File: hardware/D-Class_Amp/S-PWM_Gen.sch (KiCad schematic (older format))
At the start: 11 parts, among them U501 MAX4016, U502 Comparator_Dual_Generic

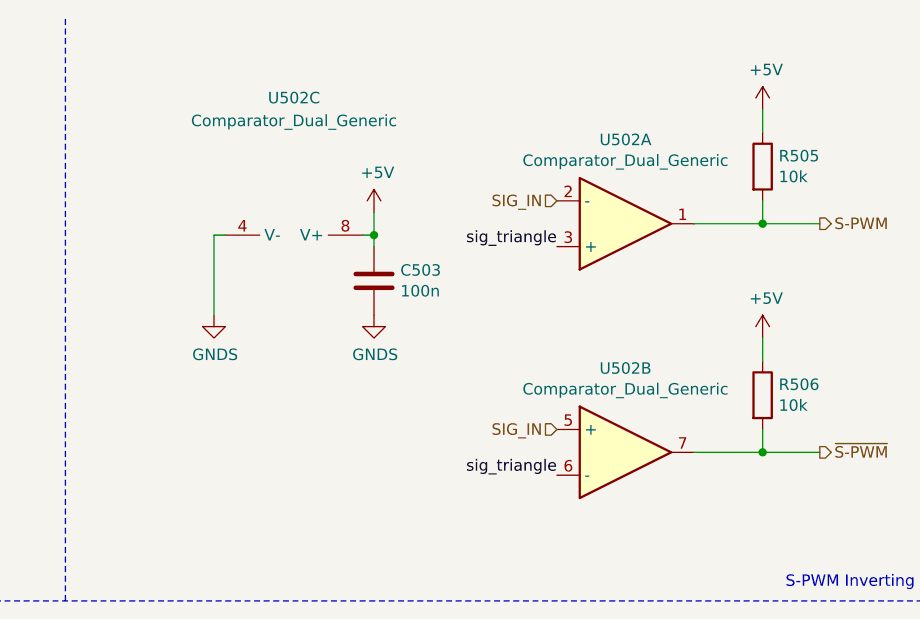
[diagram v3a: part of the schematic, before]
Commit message: select comparator and set footprint
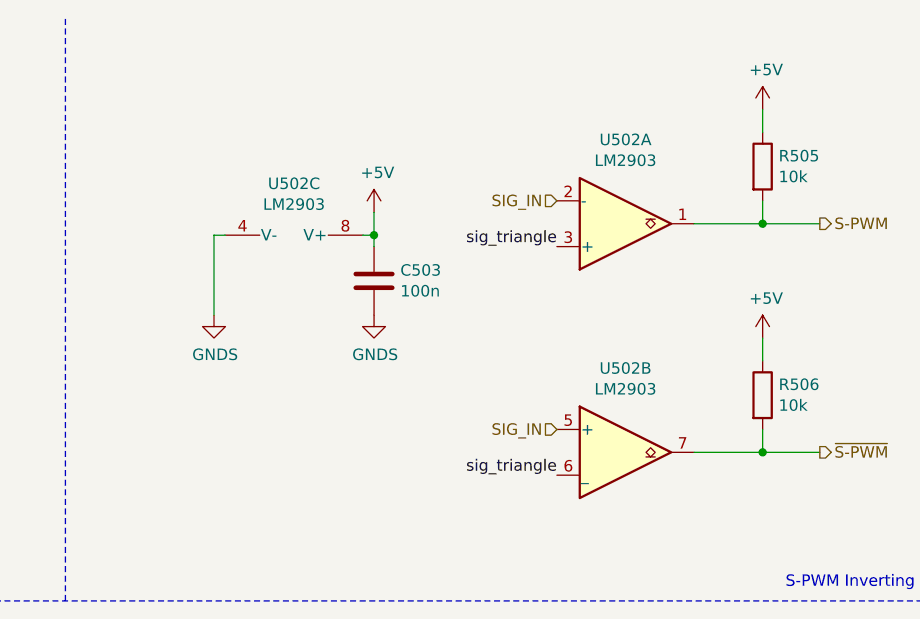
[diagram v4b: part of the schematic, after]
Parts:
- removed U502: Comparator_Dual_Generic, symbol Device:Opamp_Dual_Generic
- added U502: LM2903, Package_SO:SOIC-8_3.9x4.9mm_P1.27mm, symbol Comparator:LM2903
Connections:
- net +5V: now also U502.8 (V+)
- net GNDS: now also U502.4 (V-)
- net S-PWM: now also U502.1
- net SIG_IN: now also U502.2 (-), U502.5 (+)
- net sig_triangle: now also U502.3 (+), U502.6 (_)
- net ~S-PWM: now also U502.7
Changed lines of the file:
@@
 Text Label 5325 1925 2    50   ~ 0
 sig_triangle
-Text HLabel 9600 1375 2    50   Output ~ 0
-S-PWM
 Text HLabel 9600 2375 2    50   Output ~ 0
 ~S-PWM
-$Comp
-L Device:Opamp_Dual_Generic U502
-U 1 1 610E84D1
-P 8750 1375
-F 0 "U502" H 8750 1008 50  0000 C CNN
-F 1 "Comparator_Dual_Generic" H 8750 1099 50  0000 C CNN
-F 2 "" H 8750 1375 50  0001 C CNN
-F 3 "~" H 8750 1375 50  0001 C CNN
-	1    8750 1375
-	1    0    0    1
-$EndComp
-$Comp
-L Device:Opamp_Dual_Generic U502
-U 2 1 610E8A2F
-P 8750 2375
-F 0 "U502" H 8750 2742 50  0000 C CNN
-F 1 "Comparator_Dual_Generic" H 8750 2651 50  0000 C CNN
-F 2 "" H 8750 2375 50  0001 C CNN
-F 3 "~" H 8750 2375 50  0001 C CNN
-	2    8750 2375
-	1    0    0    -1
-$EndComp
 $Comp
 L Device:C C503
@@
 	1    0    0    -1
 $EndComp
-$Comp
-L Device:Opamp_Dual_Generic U502
-U 3 1 610E9B4A
-P 7300 1525
-F 0 "U502" V 6600 1525 50  0000 C CNN
-F 1 "Comparator_Dual_Generic" V 6700 1525 50  0000 C CNN
-F 2 "" H 7300 1525 50  0001 C CNN
-F 3 "~" H 7300 1525 50  0001 C CNN
-	3    7300 1525
-	0    1    1    0
-$EndComp
 Wire Wire Line
 	7650 1475 7650 1425
@@
 Text HLabel 8450 2275 0    50   Input ~ 0
 SIG_IN
-Text HLabel 8450 1275 0    50   Input ~ 0
-SIG_IN
-Text Label 8450 1475 2    50   ~ 0
-sig_triangle
 Text Label 8450 2475 2    50   ~ 0
 sig_triangle
-Wire Wire Line
-	9050 1375 9350 1375
-$Comp
-L Device:R R505
-U 1 1 6112AEF0
-P 9350 1125
-F 0 "R505" H 9420 1171 50  0000 L CNN
-F 1 "10k" H 9420 1080 50  0000 L CNN
-F 2 "Resistor_SMD:R_0805_2012Metric_Pad1.20x1.40mm_HandSolder" V 9280 1125 50  0001 C CNN
-F 3 "~" H 9350 1125 50  0001 C CNN
-	1    9350 1125
-	1    0    0    -1
-$EndComp
-Wire Wire Line
-	9350 1275 9350 1375
-Connection ~ 9350 1375
-Wire Wire Line
-	9350 1375 9600 1375
-$Comp
-L power:+5V #PWR0509
-U 1 1 61133A73
-P 9350 875
-F 0 "#PWR0509" H 9350 725 50  0001 C CNN
-F 1 "+5V" H 9365 1048 50  0000 C CNN
-F 2 "" H 9350 875 50  0001 C CNN
-F 3 "" H 9350 875 50  0001 C CNN
-	1    9350 875
-	1    0    0    -1
-$EndComp
-Wire Wire Line
-	9350 875  9350 975
 Wire Wire Line
 	9050 2375 9350 2375
@@
 Wire Wire Line
 	4025 2025 4075 2025
+$Comp
+L Comparator:LM2903 U502
+U 3 1 610EF685
+P 7300 1525
+F 0 "U502" V 6975 1525 50  0000 C CNN
+F 1 "LM2903" V 7066 1525 50  0000 C CNN
+F 2 "Package_SO:SOIC-8_3.9x4.9mm_P1.27mm" H 7300 1525 50  0001 C CNN
+F 3 "http://www.ti.com/lit/ds/symlink/lm393.pdf" H 7300 1525 50  0001 C CNN
+	3    7300 1525
+	0    1    1    0
+$EndComp
+$Comp
+L Comparator:LM2903 U502
+U 2 1 610F0244
+P 8750 2375
+F 0 "U502" H 8750 2742 50  0000 C CNN
+F 1 "LM2903" H 8750 2651 50  0000 C CNN
+F 2 "Package_SO:SOIC-8_3.9x4.9mm_P1.27mm" H 8750 2375 50  0001 C CNN
+F 3 "http://www.ti.com/lit/ds/symlink/lm393.pdf" H 8750 2375 50  0001 C CNN
+	2    8750 2375
+	1    0    0    -1
+$EndComp
+$Comp
+L Comparator:LM2903 U502
+U 1 1 610ED916
+P 8750 1375
+F 0 "U502" H 8750 1008 50  0000 C CNN
+F 1 "LM2903" H 8750 1099 50  0000 C CNN
+F 2 "Package_SO:SOIC-8_3.9x4.9mm_P1.27mm" H 8750 1375 50  0001 C CNN
+F 3 "http://www.ti.com/lit/ds/symlink/lm393.pdf" H 8750 1375 50  0001 C CNN
+	1    8750 1375
+	1    0    0    1
+$EndComp
+Wire Wire Line
+	9350 875  9350 975
+$Comp
+L power:+5V #PWR0509
+U 1 1 61133A73
+P 9350 875
+F 0 "#PWR0509" H 9350 725 50  0001 C CNN
+F 1 "+5V" H 9365 1048 50  0000 C CNN
+F 2 "" H 9350 875 50  0001 C CNN
+F 3 "" H 9350 875 50  0001 C CNN
+	1    9350 875
+	1    0    0    -1
+$EndComp
+Wire Wire Line
+	9350 1375 9600 1375
+Connection ~ 9350 1375
+Wire Wire Line
+	9350 1275 9350 1375
+$Comp
+L Device:R R505
+U 1 1 6112AEF0
+P 9350 1125
+F 0 "R505" H 9420 1171 50  0000 L CNN
+F 1 "10k" H 9420 1080 50  0000 L CNN
+F 2 "Resistor_SMD:R_0805_2012Metric_Pad1.20x1.40mm_HandSolder" V 9280 1125 50  0001 C CNN
+F 3 "~" H 9350 1125 50  0001 C CNN
+	1    9350 1125
+	1    0    0    -1
+$EndComp
+Wire Wire Line
+	9050 1375 9350 1375
+Text Label 8450 1475 2    50   ~ 0
+sig_triangle
+Text HLabel 8450 1275 0    50   Input ~ 0
+SIG_IN
+Text HLabel 9600 1375 2    50   Output ~ 0
+S-PWM
 $EndSCHEMATC

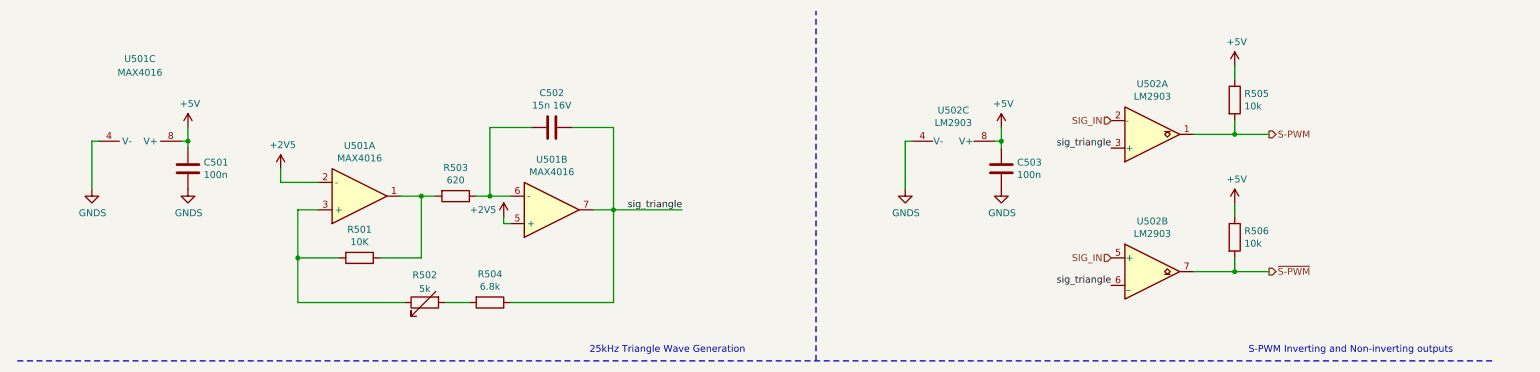
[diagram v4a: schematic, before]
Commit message: updated SPWM model with new comparators, also added test points to schematic and fixed MOSFET footprints
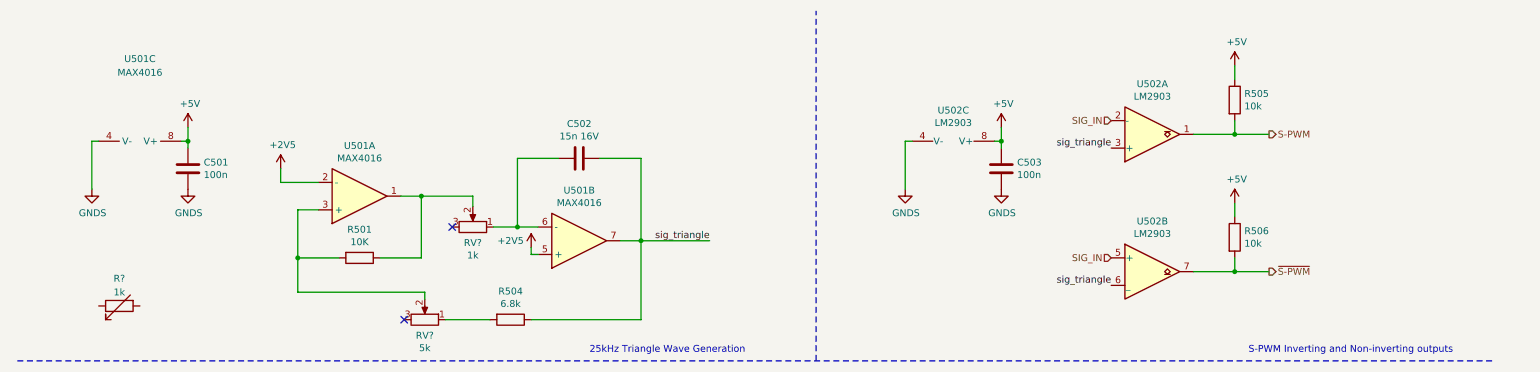
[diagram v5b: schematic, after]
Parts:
- removed R502: 5k, Potentiometer_THT:Potentiometer_Vishay_T73YP_Vertical, symbol Device:R_Variable
- removed R503: 620, Resistor_SMD:R_0805_2012Metric_Pad1.20x1.40mm_HandSolder, symbol Device:R
- added R?: 1k, Potentiometer_THT:Potentiometer_Vishay_T73YP_Vertical, symbol Device:R_Variable
- added RV?: 5k, Potentiometer_THT:Potentiometer_Vishay_T73YP_Vertical, symbol Device:R_POT
- added RV?: 1k, Potentiometer_THT:Potentiometer_Vishay_T73YP_Vertical, symbol Device:R_POT
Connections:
- net at R501.1, U501.1: now also RV?.2
- net at R501.2, U501.3 (+): now also RV?.2
- net at C502.2, U501.6 (-): now also RV?.1
- net at R504.2: now also RV?.1
- no-connect marks 0 -> 2
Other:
- moved on the sheet: C502, R504, U501B
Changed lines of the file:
@@
 $Descr A4 11693 8268
 encoding utf-8
-Sheet 5 5
+Sheet 3 5
 Title "S-PWM Generator "
 Date ""
@@
 L Device:Opamp_Dual_Generic U501
 U 2 1 6104BF37
-P 4375 1925
-F 0 "U501" H 4375 1558 50  0000 C CNN
-F 1 "MAX4016" H 4375 1649 50  0000 C CNN
-F 2 "Package_SO:SOIC-8_3.9x4.9mm_P1.27mm" H 4375 1925 50  0001 C CNN
-F 3 "https://datasheets.maximintegrated.com/en/ds/MAX4012-MAX4020.pdf" H 4375 1925 50  0001 C CNN
-	2    4375 1925
+P 4575 2150
+F 0 "U501" H 4575 1783 50  0000 C CNN
+F 1 "MAX4016" H 4575 1874 50  0000 C CNN
+F 2 "Package_SO:SOIC-8_3.9x4.9mm_P1.27mm" H 4575 2150 50  0001 C CNN
+F 3 "https://datasheets.maximintegrated.com/en/ds/MAX4012-MAX4020.pdf" H 4575 2150 50  0001 C CNN
+	2    4575 2150
 	1    0    0    1
 $EndComp
@@
 L Device:C C502
 U 1 1 610546D1
-P 4375 1325
-F 0 "C502" V 4123 1325 50  0000 C CNN
-F 1 "15n 16V" V 4214 1325 50  0000 C CNN
-F 2 "Resistor_SMD:R_0805_2012Metric_Pad1.20x1.40mm_HandSolder" H 4413 1175 50  0001 C CNN
-F 3 "~" H 4375 1325 50  0001 C CNN
-	1    4375 1325
+P 4575 1550
+F 0 "C502" V 4323 1550 50  0000 C CNN
+F 1 "15n 16V" V 4414 1550 50  0000 C CNN
+F 2 "Resistor_SMD:R_0805_2012Metric_Pad1.20x1.40mm_HandSolder" H 4613 1400 50  0001 C CNN
+F 3 "~" H 4575 1550 50  0001 C CNN
+	1    4575 1550
 	0    1    1    0
 $EndComp
@@
 	0    1    1    0
 $EndComp
-$Comp
-L Device:R R503
-U 1 1 610560D6
-P 3675 1825
-F 0 "R503" V 3468 1825 50  0000 C CNN
-F 1 "620" V 3559 1825 50  0000 C CNN
-F 2 "Resistor_SMD:R_0805_2012Metric_Pad1.20x1.40mm_HandSolder" V 3605 1825 50  0001 C CNN
-F 3 "~" H 3675 1825 50  0001 C CNN
-	1    3675 1825
-	0    1    1    0
-$EndComp
 Wire Wire Line
 	3275 1825 3425 1825
 Wire Wire Line
-	3825 1825 3925 1825
-Wire Wire Line
 	3125 2275 3425 2275
 Wire Wire Line
 	3425 2275 3425 1825
-Connection ~ 3425 1825
-Wire Wire Line
-	3425 1825 3525 1825
 Wire Wire Line
 	2825 2275 2525 2275
@@
 Wire Wire Line
 	2525 1925 2675 1925
-Connection ~ 2525 2275
-Wire Wire Line
-	4675 1925 4825 1925
+Wire Wire Line
+	4875 2150 5025 2150
 Wire Wire Line
 	2675 1725 2400 1725
 Wire Wire Line
-	4225 1325 3925 1325
-Wire Wire Line
-	3925 1325 3925 1825
-Connection ~ 3925 1825
-Wire Wire Line
-	3925 1825 4075 1825
-Wire Wire Line
-	4525 1325 4825 1325
-Wire Wire Line
-	4825 1325 4825 1925
-Connection ~ 4825 1925
+	4425 1550 4125 1550
+Wire Wire Line
+	4125 1550 4125 2050
+Connection ~ 4125 2050
+Wire Wire Line
+	4125 2050 4275 2050
+Wire Wire Line
+	4725 1550 5025 1550
+Wire Wire Line
+	5025 1550 5025 2150
+Connection ~ 5025 2150
 $Comp
 L Device:C C501
@@
 $EndComp
 Wire Wire Line
-	4825 1925 5325 1925
-Text Label 5325 1925 2    50   ~ 0
+	5025 2150 5525 2150
+Text Label 5525 2150 2    50   ~ 0
 sig_triangle
 Text HLabel 9600 2375 2    50   Output ~ 0
@@
 L Device:R R504
 U 1 1 61055E03
-P 3925 2600
-F 0 "R504" V 3718 2600 50  0000 C CNN
-F 1 "6.8k" V 3809 2600 50  0000 C CNN
-F 2 "Resistor_SMD:R_0805_2012Metric_Pad1.20x1.40mm_HandSolder" V 3855 2600 50  0001 C CNN
-F 3 "~" H 3925 2600 50  0001 C CNN
-	1    3925 2600
+P 4075 2725
+F 0 "R504" V 3868 2725 50  0000 C CNN
+F 1 "6.8k" V 3959 2725 50  0000 C CNN
+F 2 "Resistor_SMD:R_0805_2012Metric_Pad1.20x1.40mm_HandSolder" V 4005 2725 50  0001 C CNN
+F 3 "~" H 4075 2725 50  0001 C CNN
+	1    4075 2725
 	0    1    1    0
 $EndComp
-$Comp
-L Device:R_Variable R502
-U 1 1 6105EC41
-P 3450 2600
-F 0 "R502" V 3250 2600 50  0000 C CNN
-F 1 "5k" V 3350 2600 50  0000 C CNN
-F 2 "Potentiometer_THT:Potentiometer_Vishay_T73YP_Vertical" V 3380 2600 50  0001 C CNN
-F 3 "~" H 3450 2600 50  0001 C CNN
-F 4 "CT6EP102" V 3450 2600 50  0001 C CNN "Part Number"
-	1    3450 2600
-	0    -1   1    0
-$EndComp
-Wire Wire Line
-	3775 2600 3600 2600
-Wire Wire Line
-	3300 2600 2525 2600
-Wire Wire Line
-	2525 2275 2525 2600
-Wire Wire Line
-	4075 2600 4825 2600
+Wire Wire Line
+	3925 2725 3600 2725
 Text Notes 4650 2975 0    50   ~ 0
 25kHz Triangle Wave Generation
 Wire Notes Line
 	11225 3025 475  3025
-Wire Wire Line
-	4825 1925 4825 2600
 Text Notes 9450 2975 0    50   ~ 0
 S-PWM Inverting and Non-inverting outputs
@@
 L power:+2V5 #PWR0505
 U 1 1 610B2AC5
-P 4025 1975
-F 0 "#PWR0505" H 4025 1825 50  0001 C CNN
-F 1 "+2V5" H 3875 2025 50  0000 C CNN
-F 2 "" H 4025 1975 50  0001 C CNN
-F 3 "" H 4025 1975 50  0001 C CNN
-	1    4025 1975
-	1    0    0    -1
-$EndComp
-Wire Wire Line
-	4025 1975 4025 2025
-Wire Wire Line
-	4025 2025 4075 2025
+P 4225 2200
+F 0 "#PWR0505" H 4225 2050 50  0001 C CNN
+F 1 "+2V5" H 4075 2250 50  0000 C CNN
+F 2 "" H 4225 2200 50  0001 C CNN
+F 3 "" H 4225 2200 50  0001 C CNN
+	1    4225 2200
+	1    0    0    -1
+$EndComp
+Wire Wire Line
+	4225 2200 4225 2250
+Wire Wire Line
+	4225 2250 4275 2250
 $Comp
 L Comparator:LM2903 U502
@@
 Text HLabel 9600 1375 2    50   Output ~ 0
 S-PWM
+$Comp
+L Device:R_Variable R?
+U 1 1 6114CBC1
+P 1225 2625
+F 0 "R?" V 1025 2625 50  0000 C CNN
+F 1 "1k" V 1125 2625 50  0000 C CNN
+F 2 "Potentiometer_THT:Potentiometer_Vishay_T73YP_Vertical" V 1155 2625 50  0001 C CNN
+F 3 "~" H 1225 2625 50  0001 C CNN
+F 4 "CT6EP502" V 1225 2625 50  0001 C CNN "Part Number"
+	1    1225 2625
+	0    -1   1    0
+$EndComp
+$Comp
+L Device:R_POT RV?
+U 1 1 6114E136
+P 3450 2725
+F 0 "RV?" V 3335 2725 50  0000 C CNN
+F 1 "5k" V 3244 2725 50  0000 C CNN
+F 2 "Potentiometer_THT:Potentiometer_Vishay_T73YP_Vertical" H 3450 2725 50  0001 C CNN
+F 3 "~" H 3450 2725 50  0001 C CNN
+F 4 "CT6EP502" V 3450 2725 50  0001 C CNN "Part Number"
+	1    3450 2725
+	0    1    -1   0
+$EndComp
+Wire Wire Line
+	3450 2575 3450 2525
+Wire Wire Line
+	3450 2525 2525 2525
+Wire Wire Line
+	2525 2525 2525 2275
+Connection ~ 2525 2275
+NoConn ~ 3300 2725
+$Comp
+L Device:R_POT RV?
+U 1 1 611660D9
+P 3800 2050
+F 0 "RV?" V 3685 2050 50  0000 C CNN
+F 1 "1k" V 3594 2050 50  0000 C CNN
+F 2 "Potentiometer_THT:Potentiometer_Vishay_T73YP_Vertical" H 3800 2050 50  0001 C CNN
+F 3 "~" H 3800 2050 50  0001 C CNN
+F 4 "CT6EP102" V 3800 2050 50  0001 C CNN "Part Number"
+	1    3800 2050
+	0    1    -1   0
+$EndComp
+NoConn ~ 3650 2050
+Wire Wire Line
+	3425 1825 3800 1825
+Wire Wire Line
+	3800 1825 3800 1900
+Connection ~ 3425 1825
+Wire Wire Line
+	3950 2050 4125 2050
+Wire Wire Line
+	5025 2150 5025 2725
+Wire Wire Line
+	4225 2725 5025 2725
 $EndSCHEMATC

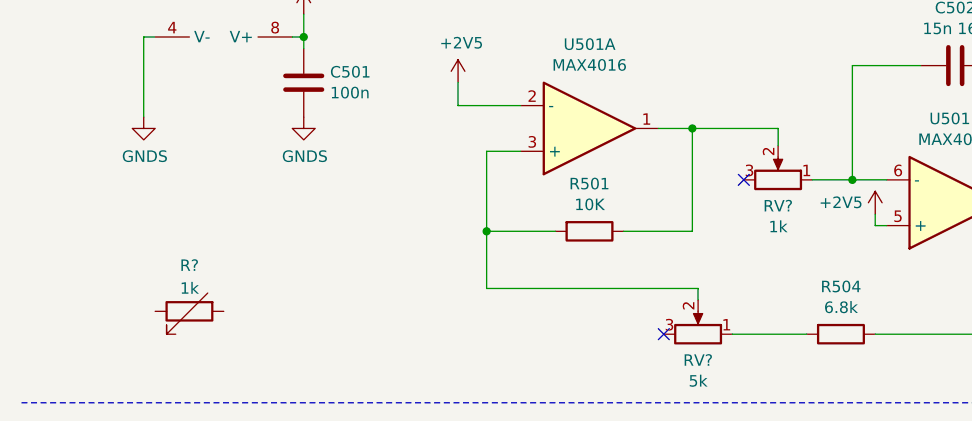
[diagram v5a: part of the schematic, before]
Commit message: Added potentiometer to input gain stage, assigned all input footprints
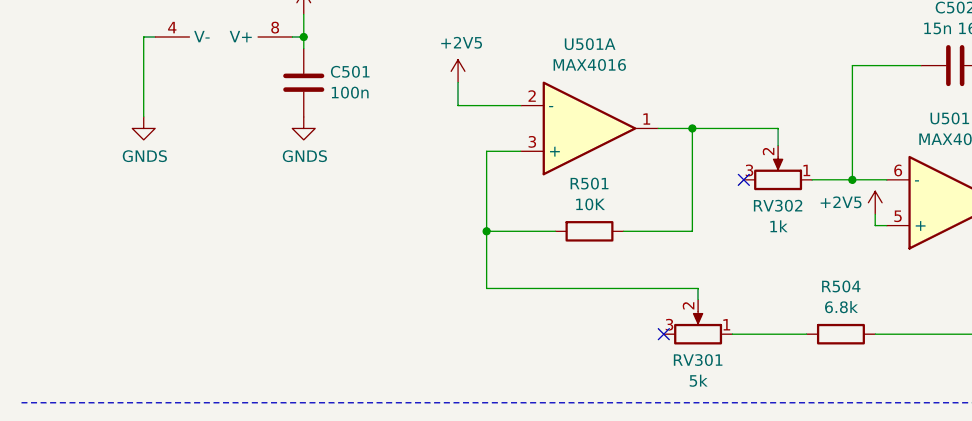
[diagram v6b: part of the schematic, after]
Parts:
- removed R?: 1k, Potentiometer_THT:Potentiometer_Vishay_T73YP_Vertical, symbol Device:R_Variable
- gave numbers to parts that had none: 2
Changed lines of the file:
@@
 S-PWM
 $Comp
-L Device:R_Variable R?
-U 1 1 6114CBC1
-P 1225 2625
-F 0 "R?" V 1025 2625 50  0000 C CNN
-F 1 "1k" V 1125 2625 50  0000 C CNN
-F 2 "Potentiometer_THT:Potentiometer_Vishay_T73YP_Vertical" V 1155 2625 50  0001 C CNN
-F 3 "~" H 1225 2625 50  0001 C CNN
-F 4 "CT6EP502" V 1225 2625 50  0001 C CNN "Part Number"
-	1    1225 2625
-	0    -1   1    0
-$EndComp
-$Comp
-L Device:R_POT RV?
+L Device:R_POT RV301
 U 1 1 6114E136
 P 3450 2725
-F 0 "RV?" V 3335 2725 50  0000 C CNN
+F 0 "RV301" V 3335 2725 50  0000 C CNN
 F 1 "5k" V 3244 2725 50  0000 C CNN
 F 2 "Potentiometer_THT:Potentiometer_Vishay_T73YP_Vertical" H 3450 2725 50  0001 C CNN
@@
 NoConn ~ 3300 2725
 $Comp
-L Device:R_POT RV?
+L Device:R_POT RV302
 U 1 1 611660D9
 P 3800 2050
-F 0 "RV?" V 3685 2050 50  0000 C CNN
+F 0 "RV302" V 3685 2050 50  0000 C CNN
 F 1 "1k" V 3594 2050 50  0000 C CNN
 F 2 "Potentiometer_THT:Potentiometer_Vishay_T73YP_Vertical" H 3800 2050 50  0001 C CNN

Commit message: added the 5V regulator and updated footprints
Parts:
- added R301, R302: 10K, Resistor_SMD:R_0805_2012Metric_Pad1.20x1.40mm_HandSolder, symbol Device:R
- added TP301: Square, symbol Connector:TestPoint
- added TP302: Triangle, symbol Connector:TestPoint
- renumbered C501 to C301, C502 to C302, C503 to C303, R501 to R303, R504 to R304, R505 to R305, R506 to R306, U501 to U301, U502 to U302
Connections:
- net +5V: now also R301.2
- net GNDS: now also R302.1
- net sig_triangle: now also TP302.1
- net at R303.1, RV302.2, U301.1: now also TP301.1
- net +2V5 renamed V_ref
- net V_ref: now also R301.1, R302.2
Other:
- moved on the sheet: C301, C302, R303, R304, RV301, RV302, U301A, U301B, U301C
